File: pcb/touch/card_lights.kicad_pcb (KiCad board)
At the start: 2 copper layers, 22.4 x 47.5 mm, 6 parts, among them SW1 SW_Push

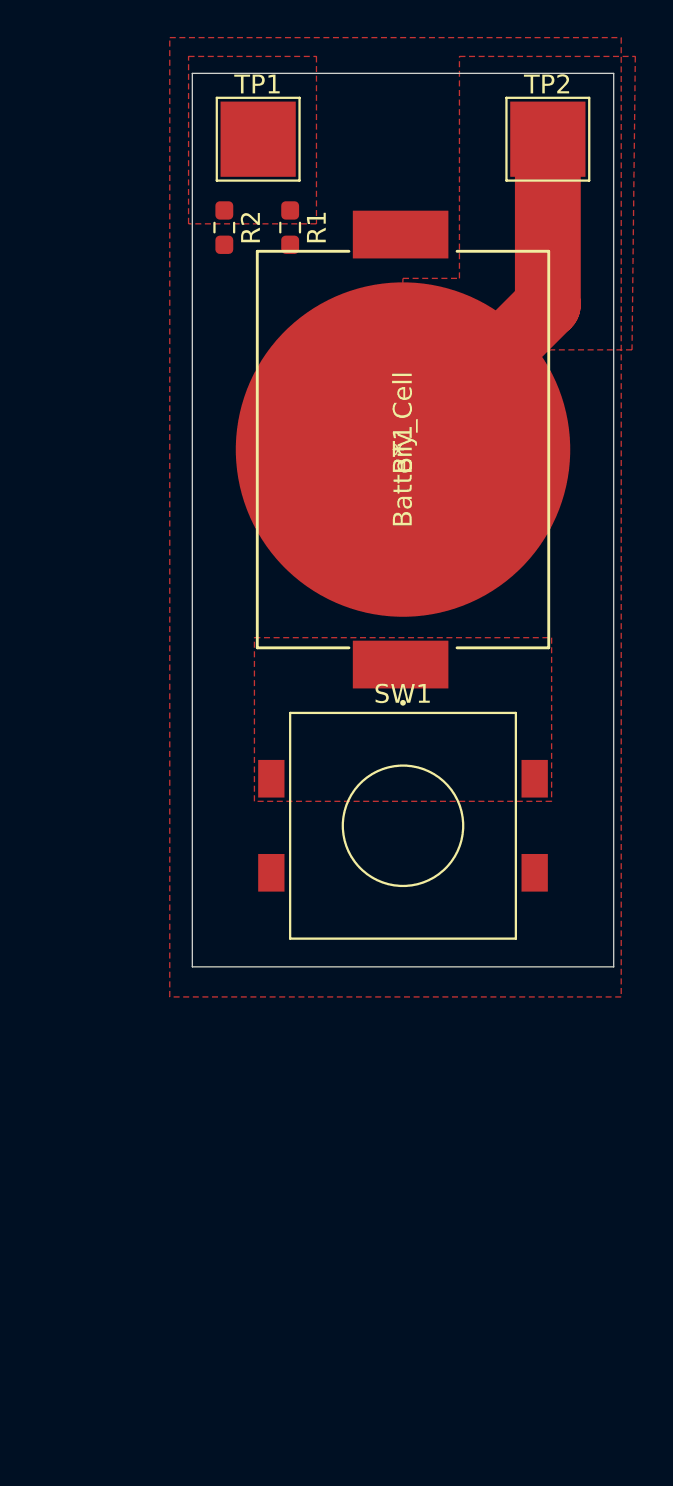
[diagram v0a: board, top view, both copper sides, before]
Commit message: create touch PCB
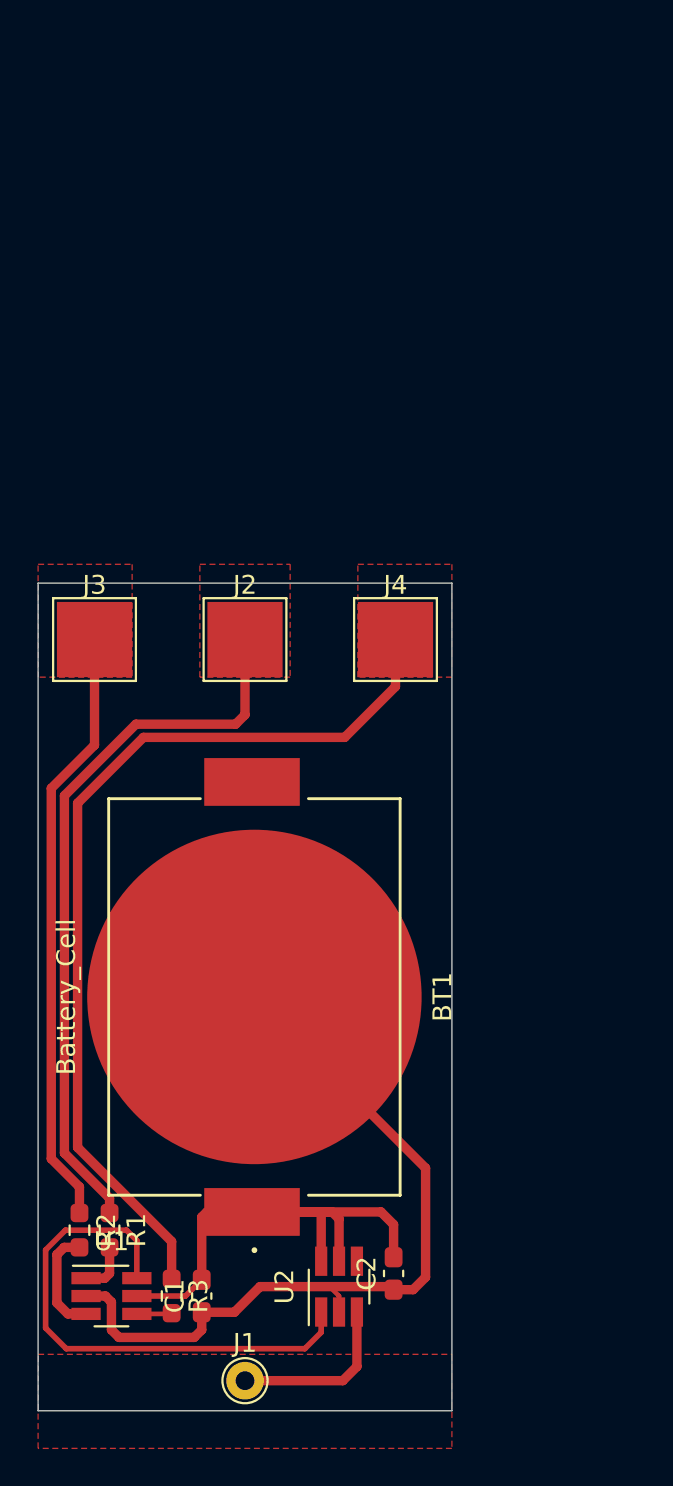
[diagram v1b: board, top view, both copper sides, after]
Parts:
- removed SW1: SW_Push, pl_Tactile_Switch_SMD:Bright_TSA123G60-250
- removed TP1, TP2: TestPoint, TestPoint:TestPoint_Pad_4.0x4.0mm
- added C1: 100n, Capacitor_SMD:C_0603_1608Metric_Pad1.08x0.95mm_HandSolder, F.Cu at (108.7, 137.9)
- added C2: 100n, Capacitor_SMD:C_0603_1608Metric_Pad1.08x0.95mm_HandSolder, F.Cu at (118.9, 136.7)
- added J1: TOUCH PAD, TestPoint:TestPoint_THTPad_D2.0mm_Drill1.0mm, F.Cu at (111.0, 142.4)
- added J2: LED_PAD, TestPoint:TestPoint_Pad_4.0x4.0mm, F.Cu at (111.0, 103.0)
- added J3: LED_PAD, TestPoint:TestPoint_Pad_4.0x4.0mm, F.Cu at (103.0, 103.0)
- added J4: LED_PAD, TestPoint:TestPoint_Pad_4.0x4.0mm, F.Cu at (119.0, 103.0)
- added R3: 91, Resistor_SMD:R_0603_1608Metric_Pad0.98x0.95mm_HandSolder, F.Cu at (107.1, 137.9)
- added U1: ATtiny10-TS, Package_TO_SOT_SMD:SOT-23-6_Handsoldering, F.Cu at (103.9, 137.9)
- added U2: TTP223E-HA6, Package_TO_SOT_SMD:SOT-23-6_Handsoldering, F.Cu at (116.0, 137.4)
- R1, R2: value 1k -> 91
- moved R1 54.2 mm to (103.8, 134.4)
- moved R2 53.9 mm to (102.2, 134.4)
- moved BT1 30.2 mm to (111.5, 122.0)
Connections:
- BT1 pad 1: Net-(BT1-Pad1) -> +3V0
- R1 pad 1: Net-(R1-Pad1) -> Net-(J2-Pad1)
- R1 pad 2: Net-(R1-Pad2) -> /PB0
- R2 pad 1: Net-(R1-Pad1) -> Net-(J3-Pad1)
- R2 pad 2: Net-(R1-Pad2) -> /PB1
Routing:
- net Net-(J4-Pad1): track 0.00 -> 49.3 mm
- net Net-(J2-Pad1): track 0.00 -> 38.6 mm
- net Net-(J3-Pad1): track 0.00 -> 32.1 mm
- net +3V0: track 0.00 -> 29.1 mm
- net /PB3: track 0.00 -> 28.2 mm
- net GND: track 19.7 -> 45.8 mm
- net /TOUCH: track 0.00 -> 9.16 mm
- net /PB1: track 0.00 -> 5.72 mm
- net /PB0: track 0.00 -> 2.74 mm
- net /PB2: track 0.00 -> 1.87 mm
- added copper zone on F.Cu, net /TOUCH
- added copper zone on F.Cu, net Net-(J2-Pad1)
- added copper zone on F.Cu, net Net-(J3-Pad1)
- added copper zone on F.Cu, net Net-(J4-Pad1)
- removed copper zone on F.Cu, net GND
- removed copper zone on F.Cu, net Net-(BT1-Pad1)
- removed copper zone on F.Cu, net Net-(R1-Pad1)
- removed copper zone on F.Cu, net Net-(R1-Pad2)
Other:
- board size 22.4 x 47.5 mm -> 22 x 44 mm

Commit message: round corners, cutout to grab coin cell
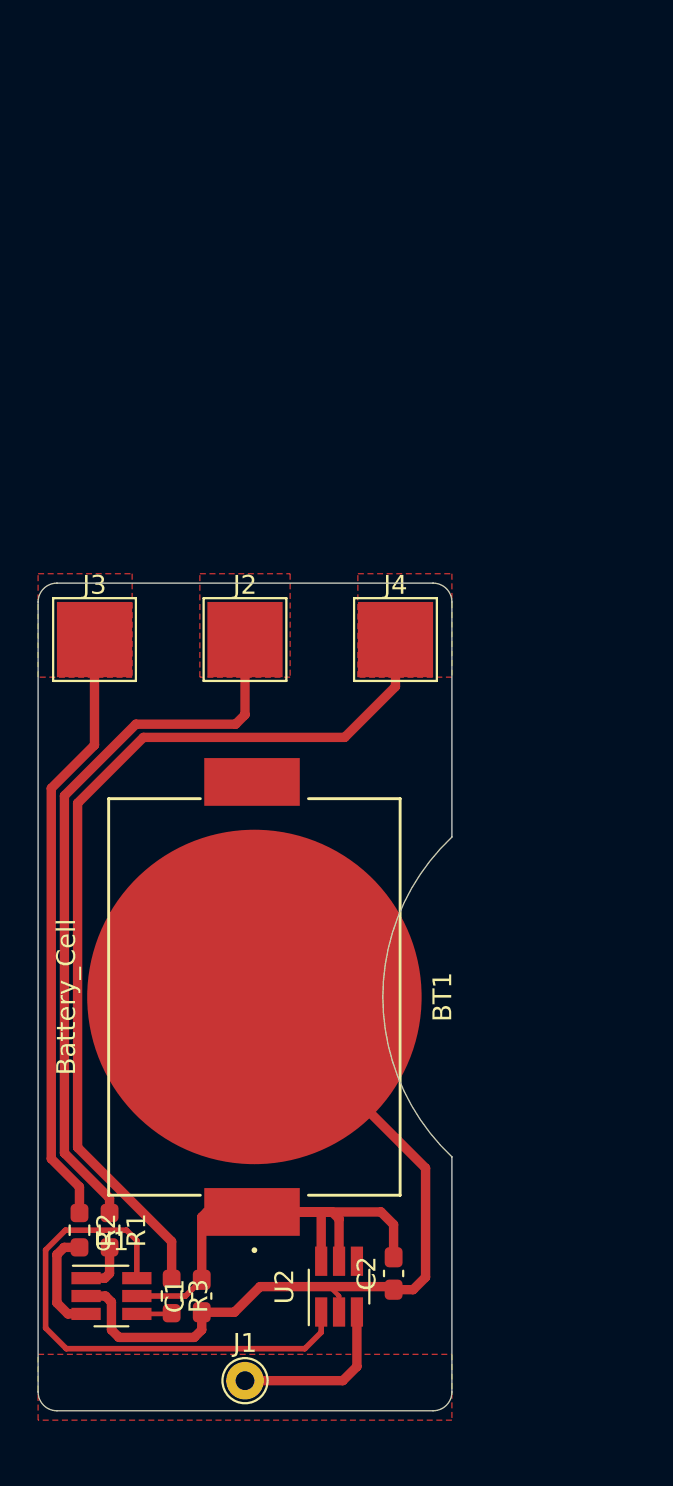
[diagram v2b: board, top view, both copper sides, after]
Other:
- outline, holes or cut-outs redrawn
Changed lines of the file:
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@@
   (general
     (thickness 1.6)
-    (drawings 4)
+    (drawings 11)
     (tracks 74)
     (zones 0)
@@
       (net 11 "Net-(J4-Pad1)"))
   )
-  (gr_line (start 100 144) (end 100 100) (layer Edge.Cuts) (width 0.05))
-  (gr_line (start 122 144) (end 100 144) (layer Edge.Cuts) (width 0.05))
-  (gr_line (start 122 100) (end 122 144) (layer Edge.Cuts) (width 0.05))
-  (gr_line (start 100 100) (end 122 100) (layer Edge.Cuts) (width 0.05))
+  (gr_arc (start 101 143) (end 100 143) (angle -90) (layer Edge.Cuts) (width 0.05))
+  (gr_arc (start 121 143) (end 121 144) (angle -90) (layer Edge.Cuts) (width 0.05))
+  (gr_arc (start 121 101) (end 122 101) (angle -90) (layer Edge.Cuts) (width 0.05))
+  (gr_arc (start 101 101) (end 101 100) (angle -90) (layer Edge.Cuts) (width 0.05))
+  (gr_line (start 122 143) (end 122 130.5) (layer Edge.Cuts) (width 0.05))
+  (gr_arc (start 130 122) (end 122 113.5) (angle -93.47140918) (layer Edge.Cuts) (width 0.05))
+  (gr_circle (center 111.5 122) (end 121.5 122) (layer Dwgs.User) (width 0.15))
+  (gr_line (start 100 143) (end 100 101) (layer Edge.Cuts) (width 0.05))
+  (gr_line (start 121 144) (end 101 144) (layer Edge.Cuts) (width 0.05))
+  (gr_line (start 122 101) (end 122 113.5) (layer Edge.Cuts) (width 0.05))
+  (gr_line (start 101 100) (end 121 100) (layer Edge.Cuts) (width 0.05))
   (segment (start 116 138.75) (end 116.05 138.75) (width 0.5) (layer F.Cu) (net 1))
   (segment (start 115.5 137.4) (end 111.8 137.4) (width 0.25) (layer F.Cu) (net 1))
@@
     (polygon
       (pts
-        (xy 113.4 105) (xy 108.6 105) (xy 108.6 99) (xy 113.4 99)
+        (xy 113.4 105) (xy 108.6 105) (xy 108.6 99.5) (xy 113.4 99.5)
       )
     )
@@
     (polygon
       (pts
-        (xy 105 105) (xy 100 105) (xy 100 99) (xy 105 99)
+        (xy 105 105) (xy 100 105) (xy 100 99.5) (xy 105 99.5)
       )
     )
@@
     (polygon
       (pts
-        (xy 122 105) (xy 117 105) (xy 117 99) (xy 122 99)
+        (xy 122 105) (xy 117 105) (xy 117 99.5) (xy 122 99.5)
       )
     )
@@
     (polygon
       (pts
-        (xy 122 146) (xy 100 146) (xy 100 141) (xy 122 141)
+        (xy 122 144.5) (xy 100 144.5) (xy 100 141) (xy 122 141)
       )
     )
